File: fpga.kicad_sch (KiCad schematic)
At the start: 36 parts, among them U201 ICE40HX4K, U202 W25Q16JV, U203 IS61WV25616FBLL-10TLI

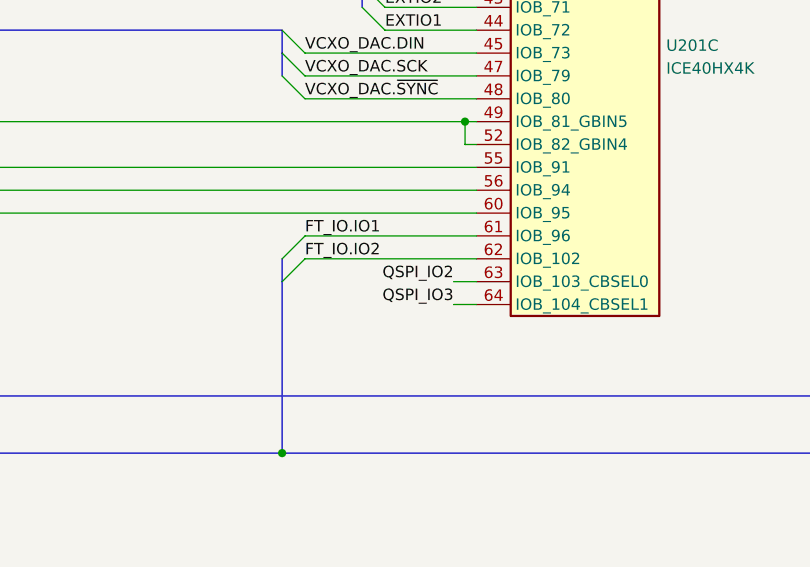
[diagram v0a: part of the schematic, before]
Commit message: FPGA: swap QSPI pins
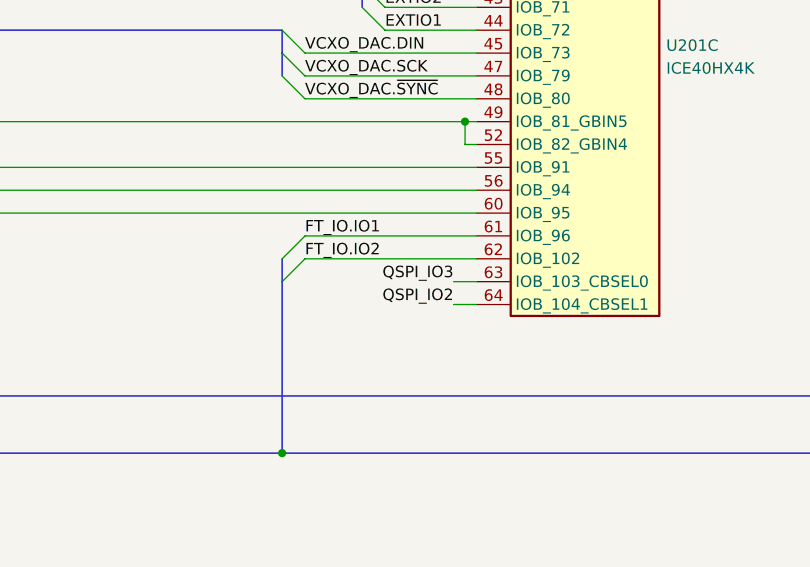
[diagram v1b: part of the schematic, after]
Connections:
- net QSPI_IO2: now also U201.64 (IOB_104_CBSEL1); no longer U201.63 (IOB_103_CBSEL0)
- net QSPI_IO3: now also U201.63 (IOB_103_CBSEL0); no longer U201.64 (IOB_104_CBSEL1)
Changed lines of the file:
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@@
     (effects (font (size 1.27 1.27)) (justify left bottom))
   )
-  (label "QSPI_IO3" (at 146.05 205.74 180)
+  (label "QSPI_IO3" (at 146.05 203.2 180)
     (effects (font (size 1.27 1.27)) (justify right bottom))
   )
@@
     (effects (font (size 1.27 1.27)) (justify right bottom))
   )
-  (label "QSPI_IO2" (at 146.05 203.2 180)
+  (label "QSPI_IO2" (at 146.05 205.74 180)
     (effects (font (size 1.27 1.27)) (justify right bottom))
   )

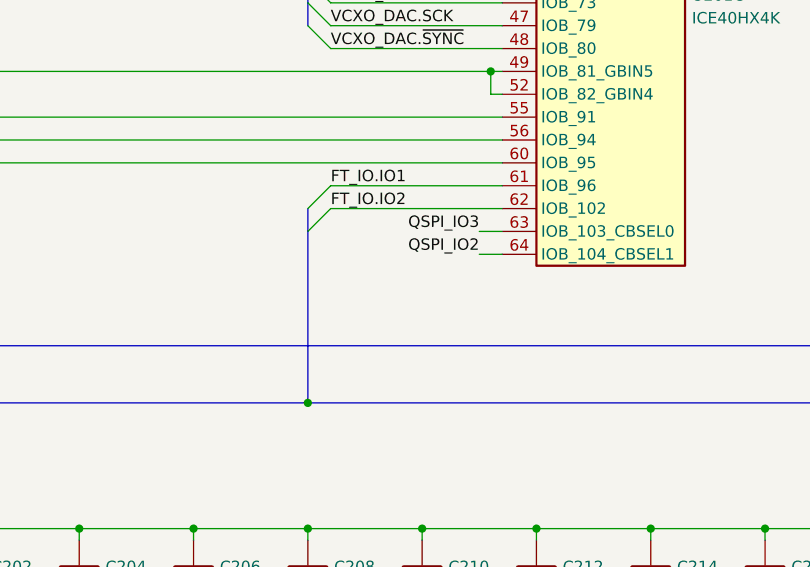
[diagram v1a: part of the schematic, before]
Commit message: Reconnect some things to simplify PCB routing
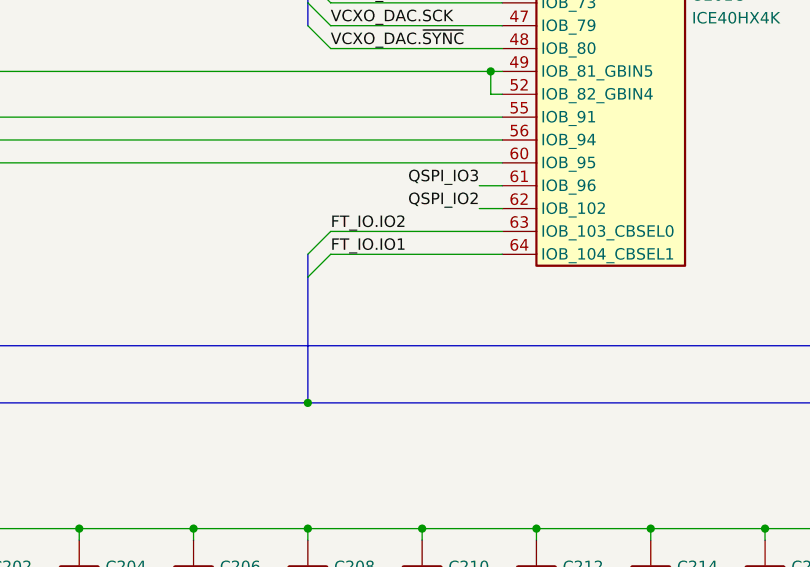
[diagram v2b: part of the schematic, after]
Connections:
- net FT_IO.IO1: now also U201.64 (IOB_104_CBSEL1); no longer U201.61 (IOB_96)
- net FT_IO.IO2: now also U201.63 (IOB_103_CBSEL0); no longer U201.62 (IOB_102)
- net QSPI_IO2: now also U201.62 (IOB_102); no longer U201.64 (IOB_104_CBSEL1)
- net QSPI_IO3: now also U201.61 (IOB_96); no longer U201.63 (IOB_103_CBSEL0)
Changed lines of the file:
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@@
     (stroke (width 0) (type default) (color 0 0 0 0))
   )
-  (bus_entry (at 127 203.2) (size 2.54 -2.54)
+  (bus_entry (at 127 208.28) (size 2.54 -2.54)
     (stroke (width 0) (type default) (color 0 0 0 0))
   )
@@
     (stroke (width 0) (type default) (color 0 0 0 0))
   )
-  (bus_entry (at 127 200.66) (size 2.54 -2.54)
+  (bus_entry (at 127 205.74) (size 2.54 -2.54)
     (stroke (width 0) (type default) (color 0 0 0 0))
   )
@@
     (stroke (width 0) (type default) (color 0 0 0 0))
   )
+  (bus (pts (xy 127 208.28) (xy 127 222.25))
+    (stroke (width 0) (type default) (color 0 0 0 0))
+  )
   (wire (pts (xy 76.2 236.22) (xy 76.2 237.49))
     (stroke (width 0) (type default) (color 0 0 0 0))
@@
     (stroke (width 0) (type default) (color 0 0 0 0))
   )
-  (bus (pts (xy 127 203.2) (xy 127 222.25))
-    (stroke (width 0) (type default) (color 0 0 0 0))
-  )
   (bus (pts (xy 254 62.23) (xy 254 64.77))
     (stroke (width 0) (type default) (color 0 0 0 0))
@@
     (stroke (width 0) (type default) (color 0 0 0 0))
   )
-  (wire (pts (xy 146.05 205.74) (xy 148.59 205.74))
+  (wire (pts (xy 146.05 200.66) (xy 148.59 200.66))
     (stroke (width 0) (type default) (color 0 0 0 0))
   )
@@
     (stroke (width 0) (type default) (color 0 0 0 0))
   )
-  (wire (pts (xy 129.54 198.12) (xy 148.59 198.12))
+  (wire (pts (xy 129.54 203.2) (xy 148.59 203.2))
     (stroke (width 0) (type default) (color 0 0 0 0))
   )
@@
     (stroke (width 0) (type default) (color 0 0 0 0))
   )
-  (wire (pts (xy 129.54 200.66) (xy 148.59 200.66))
+  (wire (pts (xy 129.54 205.74) (xy 148.59 205.74))
     (stroke (width 0) (type default) (color 0 0 0 0))
   )
@@
     (stroke (width 0) (type default) (color 0 0 0 0))
   )
+  (bus (pts (xy 127 205.74) (xy 127 208.28))
+    (stroke (width 0) (type default) (color 0 0 0 0))
+  )
   (bus (pts (xy 196.85 74.93) (xy 196.85 77.47))
     (stroke (width 0) (type default) (color 0 0 0 0))
@@
     (stroke (width 0) (type default) (color 0 0 0 0))
   )
-  (wire (pts (xy 146.05 203.2) (xy 148.59 203.2))
+  (wire (pts (xy 146.05 198.12) (xy 148.59 198.12))
     (stroke (width 0) (type default) (color 0 0 0 0))
   )
@@
   )
   (wire (pts (xy 199.39 57.15) (xy 212.09 57.15))
-    (stroke (width 0) (type default) (color 0 0 0 0))
-  )
-  (bus (pts (xy 127 200.66) (xy 127 203.2))
     (stroke (width 0) (type default) (color 0 0 0 0))
   )
@@
     (effects (font (size 1.27 1.27)) (justify left bottom))
   )
-  (label "FT_IO.IO1" (at 129.54 198.12 0)
+  (label "FT_IO.IO1" (at 129.54 205.74 0)
     (effects (font (size 1.27 1.27)) (justify left bottom))
   )
@@
     (effects (font (size 1.27 1.27)) (justify left bottom))
   )
-  (label "QSPI_IO3" (at 146.05 203.2 180)
+  (label "QSPI_IO3" (at 146.05 198.12 180)
     (effects (font (size 1.27 1.27)) (justify right bottom))
   )
@@
     (effects (font (size 1.27 1.27)) (justify right bottom))
   )
-  (label "QSPI_IO2" (at 146.05 205.74 180)
+  (label "QSPI_IO2" (at 146.05 200.66 180)
     (effects (font (size 1.27 1.27)) (justify right bottom))
   )
@@
     (effects (font (size 1.27 1.27)) (justify left bottom))
   )
-  (label "FT_IO.IO2" (at 129.54 200.66 0)
-    (effects (font (size 1.27 1.27)) (justify left bottom))
-  )
+  (label "FT_IO.IO2" (at 129.54 203.2 0)
+    (effects (font (size 1.27 1.27)) (justify left bottom))
+  )

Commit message: FPGA: remove support for SPI slave mode - Now FTDI can only talk to QSPI flash - FPGA boots exclusively from QSPI flash
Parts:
- removed JP201: FLASH/CRAM, Connector_PinHeader_2.54mm:PinHeader_2x02_P2.54mm_Vertical, symbol symbols:Jumper_4_DPDT
- removed JP202: FLASH/CRAM, Connector_PinHeader_2.54mm:PinHeader_1x02_P2.54mm_Vertical, symbol symbols:Jumper_2
- removed R201: 220, Resistor_SMD:R_0805_2012Metric, symbol Device:R
- renumbered R202 to R201, R203 to R202, R204 to R203, R205 to R204, R206 to R205, R207 to R206, R208 to R207
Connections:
- net FT_SPI.MISO: now also U201.68 (IOB_106_SDI), U202.2 (DO/IO1)
- net FT_SPI.MOSI: now also U201.67 (IOB_105_SDO), U202.5 (DI/IO0)
- net FT_SPI.~{CS}: now also R201.2, U202.1 (~{CS})
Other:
- moved on the sheet: C222, C223, R201, R202, R203, R207

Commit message: FPGA: swap CLK_OUT and CLK_SEL
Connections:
- net CLK_OUT: now also U201.55 (IOB_91); no longer U201.56 (IOB_94)
- net CLK_OUT_SEL: now also U201.56 (IOB_94); no longer U201.55 (IOB_91)
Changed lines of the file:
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@@
     (effects (font (size 1.27 1.27)) (justify right))
   )
-  (hierarchical_label "CLK_OUT" (shape output) (at 76.2 193.04 180)
+  (hierarchical_label "CLK_OUT" (shape output) (at 76.2 190.5 180)
     (effects (font (size 1.27 1.27)) (justify right))
   )
@@
     (effects (font (size 1.27 1.27)) (justify right))
   )
-  (hierarchical_label "CLK_OUT_SEL" (shape output) (at 76.2 190.5 180)
+  (hierarchical_label "CLK_OUT_SEL" (shape output) (at 76.2 193.04 180)
     (effects (font (size 1.27 1.27)) (justify right))
   )

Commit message: Update schematic: - Redesign of decoupling based on swcad modelling (predominantly use 1uf, no paralleled caps) - Reroute REF_CLK_IN, CLK_SEL net to different FPGA pins - Some net renaming - Ext conn: add decoupling to 3v3 output - Reassign references to all components PCB: routing almost finished
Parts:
- removed C215, C216, C217, C218, C219: 100n, Capacitor_SMD:C_0805_2012Metric, symbol Device:C
- C201, C202, C203: value 4.7u -> 1u; Mfr Murata -> Samsung; Mfr PN GRM21BR71C475ME51 -> CL21B105KOFNNNG
- C204, C206, C207, C208, C209, C210, C211, C212, C213, C214: value 100n -> 1u; Mfr PN CL21B104KBFNNNE -> CL21B105KOFNNNG
- renumbered C220 to C215, C221 to C216, C222 to C217, C223 to C218
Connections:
- net +1.2VD: no longer C211.1, C213.1
- net +3.3VD: now also C211.1, C213.1
- net CLK_OUT_SEL: now also U201.60 (IOB_95); no longer U201.56 (IOB_94)
- net REF_CLK_IN: now also U201.56 (IOB_94); no longer U201.60 (IOB_95)

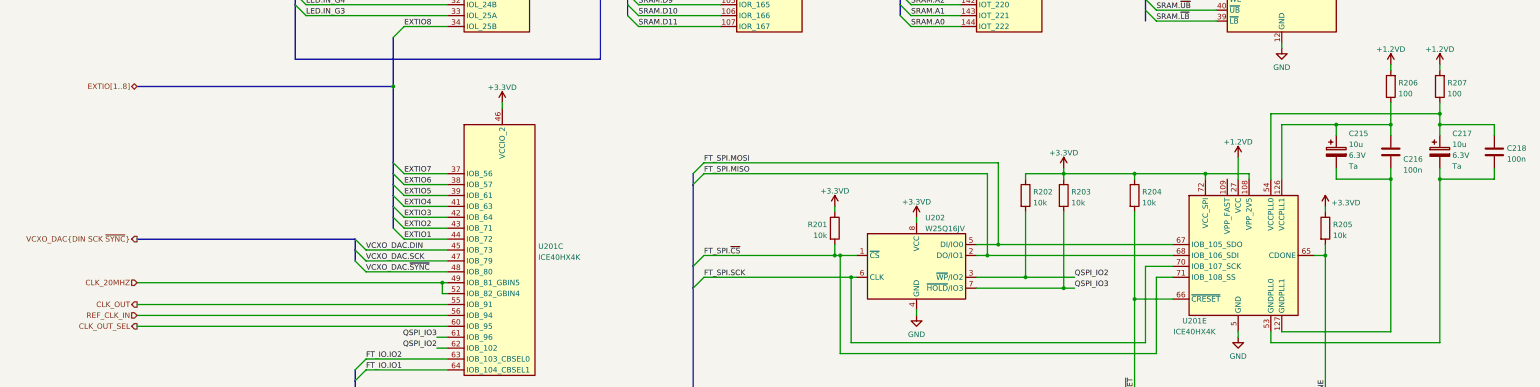
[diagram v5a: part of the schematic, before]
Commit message: - Add matching / anti-ring resistors to clock nets - Use 0603 resistors for anti-ring - Improve CLK_OUT routing
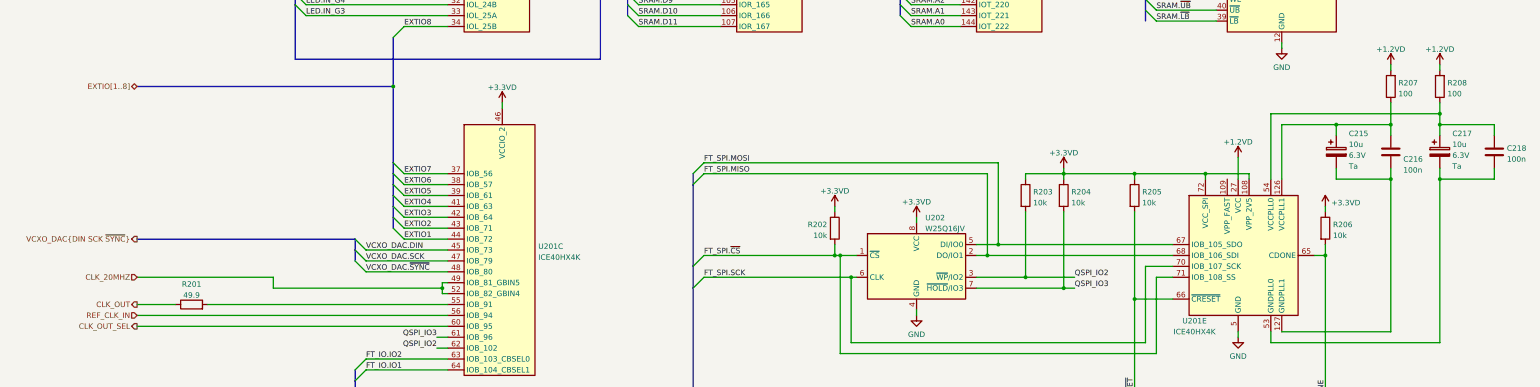
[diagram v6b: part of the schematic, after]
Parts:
- added R201: 49.9, Resistor_SMD:R_0603_1608Metric, symbol Device:R
- renumbered R201 to R202, R202 to R203, R203 to R204, R204 to R205, R205 to R206, R206 to R207, R207 to R208
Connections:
- net CLK_OUT: now also R201.1; no longer U201.55 (IOB_91)
- new net: R201.2, U201.55 (IOB_91)
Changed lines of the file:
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@@
   (junction (at 139.7 246.38) (diameter 0) (color 0 0 0 0)
   )
+  (junction (at 147.32 186.69) (diameter 0) (color 0 0 0 0)
+  )
   (junction (at 353.06 179.07) (diameter 0) (color 0 0 0 0)
   )
@@
   (junction (at 379.73 161.29) (diameter 0) (color 0 0 0 0)
   )
-  (junction (at 147.32 185.42) (diameter 0) (color 0 0 0 0)
-  )
   (junction (at 242.57 184.15) (diameter 0) (color 0 0 0 0)
   )
@@
     (stroke (width 0) (type default) (color 0 0 0 0))
   )
+  (wire (pts (xy 92.71 190.5) (xy 148.59 190.5))
+    (stroke (width 0) (type default) (color 0 0 0 0))
+  )
   (wire (pts (xy 212.09 110.49) (xy 193.04 110.49))
     (stroke (width 0) (type default) (color 0 0 0 0))
@@
     (stroke (width 0) (type default) (color 0 0 0 0))
   )
-  (wire (pts (xy 76.2 190.5) (xy 148.59 190.5))
+  (wire (pts (xy 76.2 190.5) (xy 85.09 190.5))
     (stroke (width 0) (type default) (color 0 0 0 0))
   )
@@
     (stroke (width 0) (type default) (color 0 0 0 0))
   )
-  (wire (pts (xy 147.32 187.96) (xy 147.32 185.42))
+  (wire (pts (xy 147.32 187.96) (xy 147.32 186.69))
     (stroke (width 0) (type default) (color 0 0 0 0))
   )
@@
     (stroke (width 0) (type default) (color 0 0 0 0))
   )
+  (wire (pts (xy 147.32 186.69) (xy 147.32 185.42))
+    (stroke (width 0) (type default) (color 0 0 0 0))
+  )
   (bus (pts (xy 133.35 62.23) (xy 133.35 59.69))
     (stroke (width 0) (type default) (color 0 0 0 0))
@@
     (stroke (width 0) (type default) (color 0 0 0 0))
   )
+  (wire (pts (xy 107.95 184.15) (xy 107.95 186.69))
+    (stroke (width 0) (type default) (color 0 0 0 0))
+  )
   (wire (pts (xy 256.54 115.57) (xy 267.97 115.57))
     (stroke (width 0) (type default) (color 0 0 0 0))
@@
     (stroke (width 0) (type default) (color 0 0 0 0))
   )
+  (wire (pts (xy 76.2 184.15) (xy 107.95 184.15))
+    (stroke (width 0) (type default) (color 0 0 0 0))
+  )
   (wire (pts (xy 101.6 261.62) (xy 88.9 261.62))
     (stroke (width 0) (type default) (color 0 0 0 0))
@@
     (stroke (width 0) (type default) (color 0 0 0 0))
   )
+  (wire (pts (xy 107.95 186.69) (xy 147.32 186.69))
+    (stroke (width 0) (type default) (color 0 0 0 0))
+  )
   (wire (pts (xy 135.89 57.15) (xy 148.59 57.15))
     (stroke (width 0) (type default) (color 0 0 0 0))
@@
     (stroke (width 0) (type default) (color 0 0 0 0))
   )
-  (wire (pts (xy 76.2 185.42) (xy 147.32 185.42))
-    (stroke (width 0) (type default) (color 0 0 0 0))
-  )
   (bus (pts (xy 311.15 48.26) (xy 374.65 48.26))
     (stroke (width 0) (type default) (color 0 0 0 0))
@@
     (effects (font (size 1.27 1.27)) (justify right))
   )
-  (hierarchical_label "CLK_20MHZ" (shape input) (at 76.2 185.42 180)
+  (hierarchical_label "CLK_20MHZ" (shape input) (at 76.2 184.15 180)
     (effects (font (size 1.27 1.27)) (justify right))
   )
@@
   (symbol (lib_id "Device:R") (at 283.21 165.1 0) (unit 1)
     (in_bom yes) (on_board yes) (fields_autoplaced)
-    (property "Reference" "R202" (id 0) (at 284.988 164.2653 0)
+    (property "Reference" "R203" (id 0) (at 284.988 164.2653 0)
       (effects (font (size 1.27 1.27)) (justify left))
     )
@@
   (symbol (lib_id "Device:R") (at 379.73 139.7 180) (unit 1)
     (in_bom yes) (on_board yes) (fields_autoplaced)
-    (property "Reference" "R207" (id 0) (at 381.508 138.8653 0)
+    (property "Reference" "R208" (id 0) (at 381.508 138.8653 0)
       (effects (font (size 1.27 1.27)) (justify right))
     )
@@
     (pin "2")
   )
+  (symbol (lib_id "Device:R") (at 88.9 190.5 90) (unit 1)
+    (in_bom yes) (on_board yes) (fields_autoplaced)
+    (property "Reference" "R201" (id 0) (at 88.9 185.7842 90))
+    (property "Value" "49.9" (id 1) (at 88.9 188.3211 90))
+    (property "Footprint" "Resistor_SMD:R_0603_1608Metric" (id 2) (at 88.9 192.278 90)
+      (effects (font (size 1.27 1.27)) hide)
+    )
+    (property "Datasheet" "~" (id 3) (at 88.9 190.5 0)
+      (effects (font (size 1.27 1.27)) hide)
+    )
+    (property "Mfr" "Bourns" (id 4) (at 88.9 190.5 0)
+      (effects (font (size 1.27 1.27)) hide)
+    )
+    (property "Mfr PN" "CR0603-FX-49R9ELF" (id 5) (at 88.9 190.5 0)
+      (effects (font (size 1.27 1.27)) hide)
+    )
+    (pin "1")
+    (pin "2")
+  )
   (symbol (lib_id "Device:C") (at 127 241.3 0) (unit 1)
     (in_bom yes) (on_board yes) (fields_autoplaced)
@@
   (symbol (lib_id "Device:R") (at 308.61 165.1 0) (unit 1)
     (in_bom yes) (on_board yes) (fields_autoplaced)
-    (property "Reference" "R204" (id 0) (at 310.388 164.2653 0)
+    (property "Reference" "R205" (id 0) (at 310.388 164.2653 0)
       (effects (font (size 1.27 1.27)) (justify left))
     )
@@
   (symbol (lib_id "Device:R") (at 368.3 139.7 180) (unit 1)
     (in_bom yes) (on_board yes) (fields_autoplaced)
-    (property "Reference" "R206" (id 0) (at 370.078 138.8653 0)
+    (property "Reference" "R207" (id 0) (at 370.078 138.8653 0)
       (effects (font (size 1.27 1.27)) (justify right))
     )
@@
   (symbol (lib_id "Device:R") (at 292.1 165.1 0) (unit 1)
     (in_bom yes) (on_board yes) (fields_autoplaced)
-    (property "Reference" "R203" (id 0) (at 293.878 164.2653 0)
+    (property "Reference" "R204" (id 0) (at 293.878 164.2653 0)
       (effects (font (size 1.27 1.27)) (justify left))
     )
@@
   (symbol (lib_id "Device:R") (at 353.06 172.72 0) (unit 1)
     (in_bom yes) (on_board yes) (fields_autoplaced)
-    (property "Reference" "R205" (id 0) (at 354.838 171.8853 0)
+    (property "Reference" "R206" (id 0) (at 354.838 171.8853 0)
       (effects (font (size 1.27 1.27)) (justify left))
     )
@@
   (symbol (lib_id "Device:R") (at 238.76 172.72 0) (unit 1)
     (in_bom yes) (on_board yes) (fields_autoplaced)
-    (property "Reference" "R201" (id 0) (at 236.982 171.8853 0)
+    (property "Reference" "R202" (id 0) (at 236.982 171.8853 0)
       (effects (font (size 1.27 1.27)) (justify right))
     )
